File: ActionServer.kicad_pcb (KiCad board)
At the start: 2 copper layers, 65 x 56 mm, 23 parts, among them J1 GPIO, J2 Relay Pins 1, J3 Relay Pins 2, J4 Status Leds 1, J5 Status Leds 2, U2 ULN2003, U3 ULN2003

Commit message: CHANGE: Add plots folder
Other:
- board text added: "Modern Industry Pi Buffer Board V 0.1"

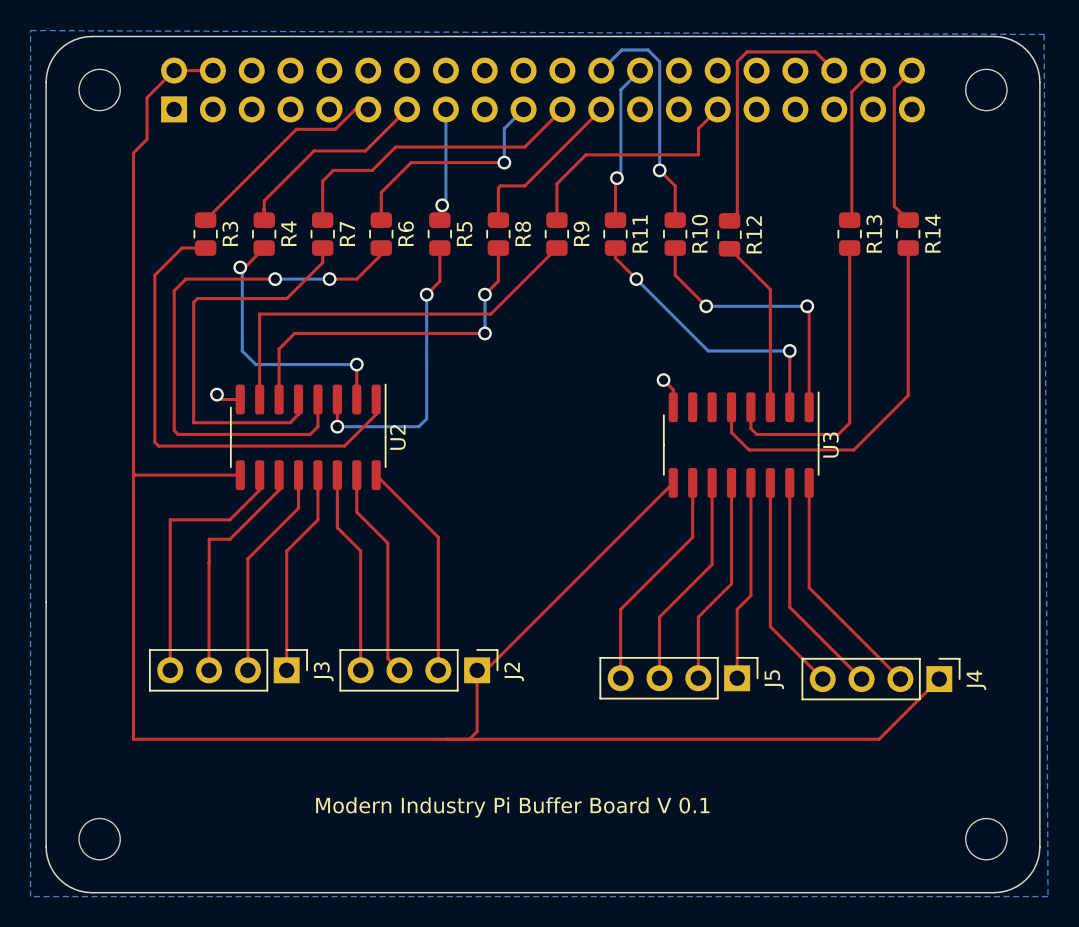
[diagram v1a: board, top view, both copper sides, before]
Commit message: FIX: Output plot options
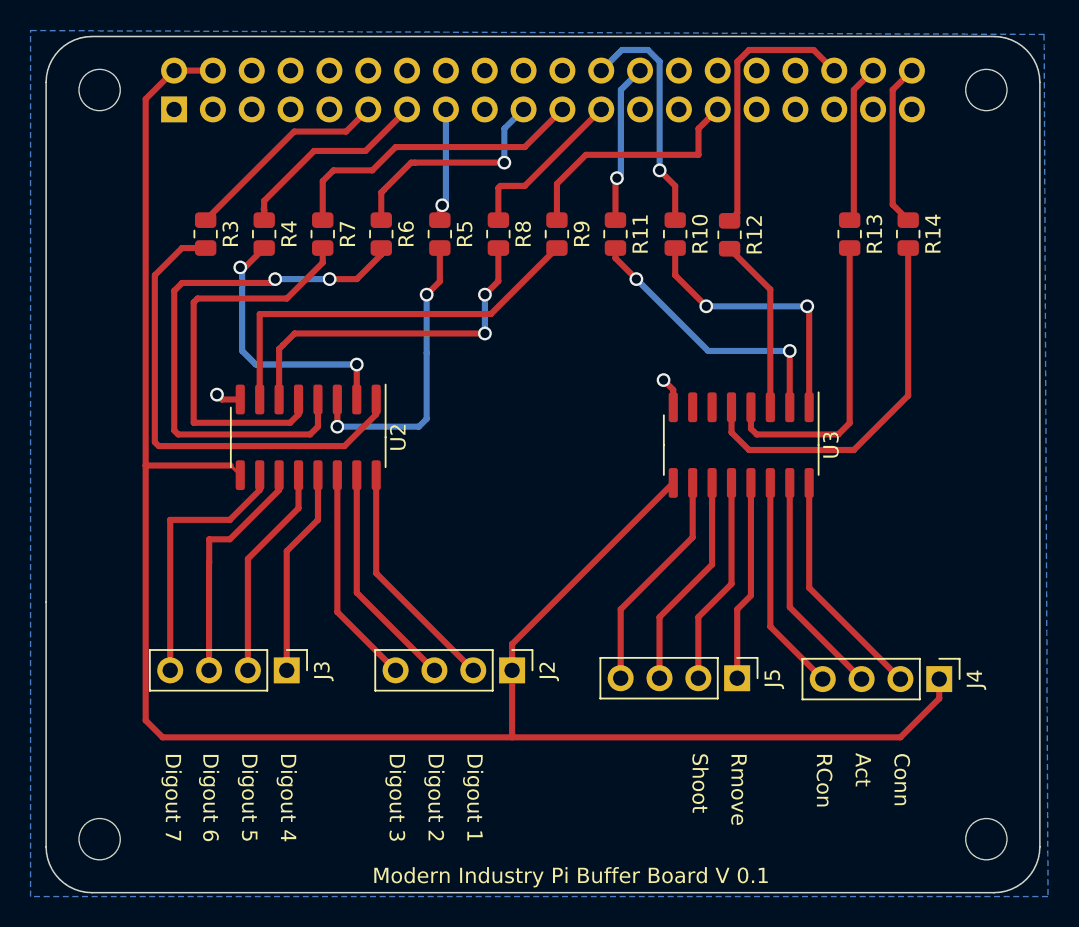
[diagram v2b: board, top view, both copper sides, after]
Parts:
- moved J2 2.29 mm to (130.5, 85.5)
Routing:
- net +5V: track 134.2 -> 129.3 mm
- net Net-(J2-Pin_4): track 13.4 -> 14.3 mm
- net Net-(J2-Pin_2): track 14.4 -> 15.4 mm
- net Net-(J2-Pin_3): track 13.9 -> 14.9 mm
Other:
- board text added: "Act"
- board text added: "Conn"
- board text added: "Digout 1"
- board text added: "Digout 2"
- board text added: "Digout 3"
- board text added: "Digout 4"
- board text added: "Digout 5"
- board text added: "Digout 6"
- board text added: "Digout 7"
- board text added: "RCon"
- board text added: "Rmove"
- board text added: "Shoot"
- board text removed: "USB"
